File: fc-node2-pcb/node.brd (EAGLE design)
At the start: 50 x 24 mm, 16 parts, among them IC1 HTU21D, J1 AVR_SPI_PRG_62X3_LOCK

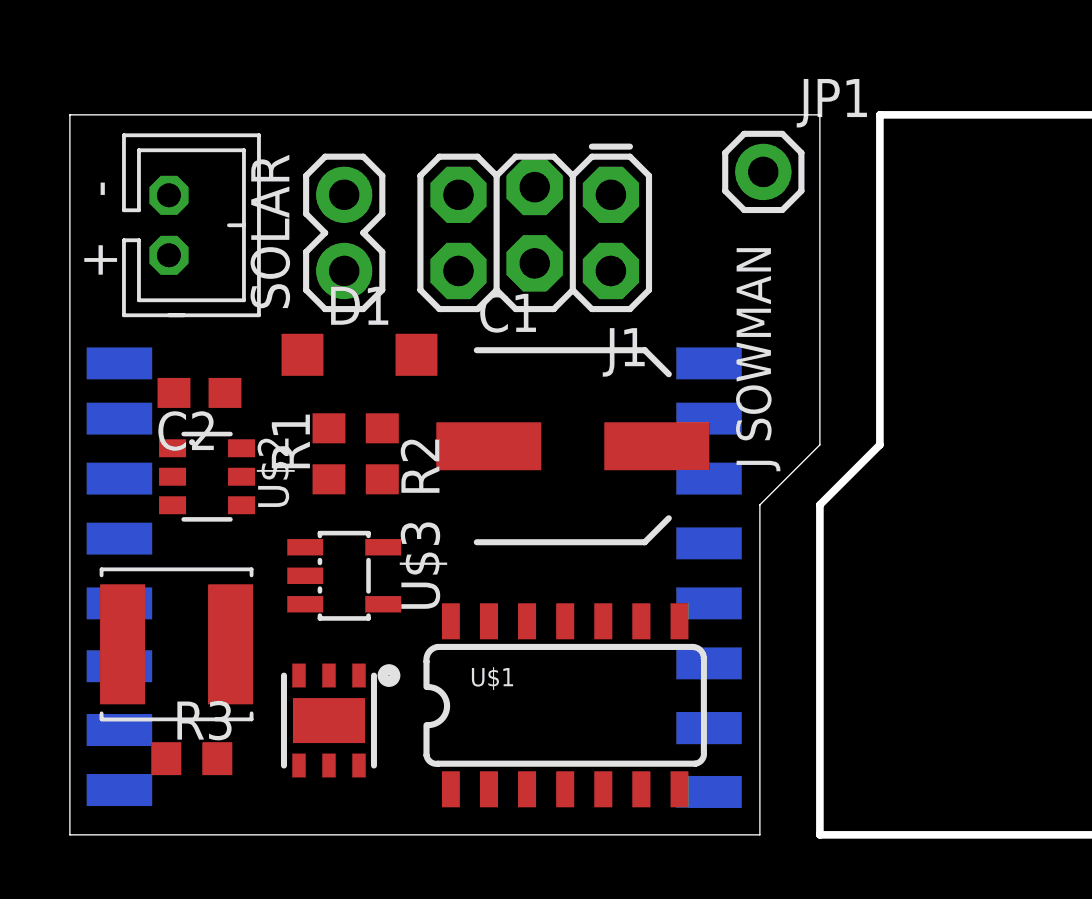
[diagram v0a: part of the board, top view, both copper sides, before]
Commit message: reduced to 23mm, begin routing fc2
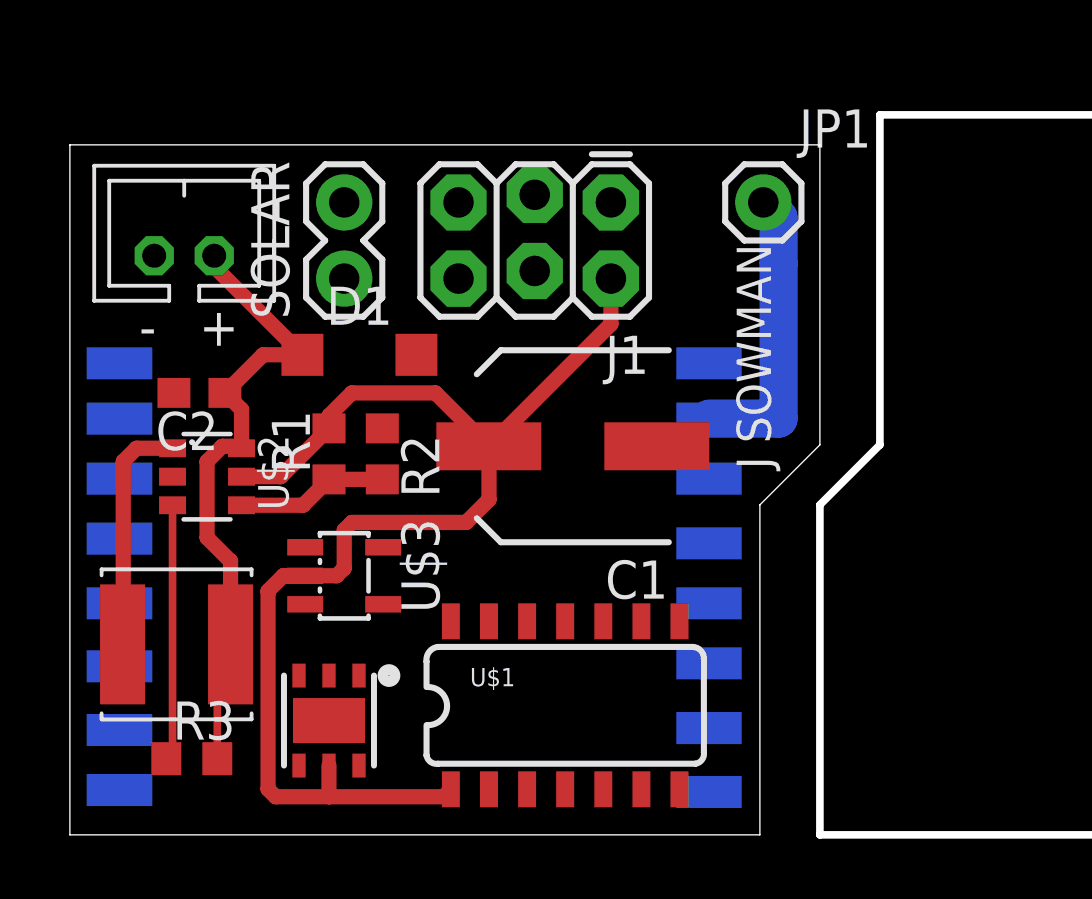
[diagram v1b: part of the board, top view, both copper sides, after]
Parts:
- moved J2 1.14 mm to (3.81, 19.3), turned to 0 degrees
- moved JP1 1.02 mm to (23.1, 21.1)
- moved J1 0.25 mm to (18.0, 21.1)
- moved SOLAR 0.25 mm to (9.14, 18.5)
- turned C1 to 180 degrees
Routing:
- net VCC: track 0.00 -> 43.5 mm
- net VBATT: track 0.00 -> 21.5 mm
- net N$3: track 0.00 -> 9.74 mm
- net EN: track 0.07 -> 8.60 mm
- net N$1: track 0.33 -> 8.26 mm
- net N$2: track 0.00 -> 5.05 mm
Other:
- outline, holes or cut-outs redrawn

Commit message: routed fc2
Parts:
- moved U$3 1.02 mm to (10.2, 8.64), turned to 180 degrees
- moved IC1 0.92 mm to (9.40, 4.32)
- moved U$1 0.51 mm to (16.5, 4.83)
- moved J1 0.51 mm to (18.0, 20.6)
- moved R1 0.25 mm to (8.64, 13.0)
- moved R2 0.25 mm to (10.4, 13.0)
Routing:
- net MOSI: track 0.00 -> 50.5 mm, vias 0 -> 2
- net SCK: track 0.00 -> 50.3 mm, vias 0 -> 2
- net RESET: track 0.00 -> 25.6 mm
- net EN: track 8.60 -> 33.6 mm
- net MISO: track 0.00 -> 21.5 mm, vias 0 -> 1
- net DIO0: track 0.00 -> 20.7 mm, vias 0 -> 1
- net VCC: track 43.5 -> 60.8 mm
- net VBATT: track 21.5 -> 37.9 mm
- net DET: track 0.00 -> 16.0 mm
- net RFM_SS: track 0.00 -> 9.28 mm, vias 0 -> 1
- net N$5: track 0.00 -> 3.54 mm
- net GND: track 0.00 -> 1.36 mm, vias 0 -> 29
- net N$3: track 9.74 -> 8.58 mm
- added copper zone on layer 1, net GND
- added copper zone on layer 16, net GND
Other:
- outline, holes or cut-outs redrawn
- board text added: "APRIL 2015"
- board text added: "J. SOWMAN"
- board text added: "JON SOWMAN"
- board text added: "UKHASnet"
- board text added: "ukhas.net"

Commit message: fc2 decoupling cap
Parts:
- added C3: 100n, rcl:C0603
- moved R3 1.27 mm to (4.06, 3.81)
- moved DF 1.02 mm to (3.56, 7.37)
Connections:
- net GND: now also C3.2
- net VCC: now also C3.1
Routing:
- net GND: track 1.36 -> 5.75 mm, vias 29 -> 32
- net EN: track 33.6 -> 35.6 mm
- net N$1: track 8.26 -> 6.92 mm
- net VBATT: track 37.9 -> 39.2 mm
- net VCC: track 60.8 -> 61.9 mm
- net SCK: track 50.3 -> 49.6 mm
- net MOSI: track 50.5 -> 49.9 mm
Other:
- board text added: "+"
- board text added: "APR 15"
- board text added: "JON"
- board text added: "SOWMAN"
- board text added: "UKHAS"
- board text removed: "J. SOWMAN"
- board text removed: "UKHASnet"

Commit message: fc2 running ok, no rfm yet
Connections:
- new net N$4: U$1.3
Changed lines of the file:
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@@
 <?xml version="1.0" encoding="utf-8"?>
 <!DOCTYPE eagle SYSTEM "eagle.dtd">
-<eagle version="6.6.0">
+<eagle version="6.5.0">
 <drawing>
 <settings>
@@
 <setting verticaltext="up"/>
 </settings>
-<grid distance="0.01" unitdist="inch" unit="inch" style="lines" multiple="1" display="yes" altdistance="0.005" altunitdist="inch" altunit="inch"/>
+<grid distance="0.05" unitdist="inch" unit="inch" style="lines" multiple="1" display="yes" altdistance="0.005" altunitdist="inch" altunit="inch"/>
 <layers>
 <layer number="1" name="Top" color="4" fill="1" visible="yes" active="yes"/>
@@
 <layer number="47" name="Measures" color="7" fill="1" visible="no" active="yes"/>
 <layer number="48" name="Document" color="7" fill="1" visible="no" active="yes"/>
-<layer number="49" name="Reference" color="7" fill="1" visible="yes" active="yes"/>
+<layer number="49" name="Reference" color="7" fill="1" visible="no" active="yes"/>
 <layer number="50" name="dxf" color="7" fill="1" visible="no" active="no"/>
 <layer number="51" name="tDocu" color="6" fill="1" visible="yes" active="yes"/>
@@
 <wire x1="11.557" y1="9.017" x2="12.446" y2="9.906" width="0.254" layer="1"/>
 </signal>
+<signal name="N$4">
+<contactref element="U$1" pad="3"/>
+</signal>
 </signals>

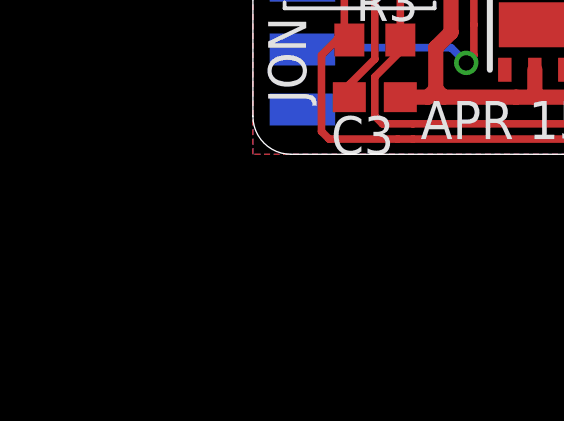
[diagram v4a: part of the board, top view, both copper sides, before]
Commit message: Work on bitbanged firmware for a attiny node
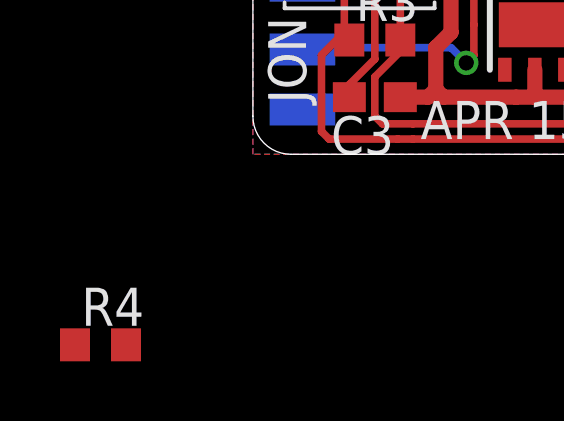
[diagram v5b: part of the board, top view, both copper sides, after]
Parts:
- added R4: (no value), rcl:R0603
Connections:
- new net N$6: U$1.6
- new net N$7: U$4.RESET
- net RFM_SS: now also R4.1
- net VCC: now also R4.2
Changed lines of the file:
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@@
 <element name="IC1" library="Mine" package="DFN6-L" value="HTU21D" x="9.398" y="4.318" rot="R180"/>
 <element name="C3" library="rcl" package="C0603" value="100n" x="4.064" y="1.905" rot="R180"/>
+<element name="R4" library="rcl" package="R0603" value="" x="-5.08" y="-6.35"/>
 </elements>
 <signals>
@@
 <wire x1="4.914" y1="1.905" x2="5.842" y2="1.905" width="0.508" layer="1"/>
 <wire x1="5.842" y1="1.905" x2="6.096" y2="2.159" width="0.508" layer="1"/>
+<contactref element="R4" pad="2"/>
+<wire x1="4.914" y1="1.905" x2="-4.23" y2="-6.35" width="0" layer="19" extent="1-1"/>
 </signal>
 <signal name="N$1">
@@
 <via x="16.51" y="3.556" extent="1-16" drill="0.508"/>
 <wire x1="16.51" y1="3.556" x2="16.51" y2="7.626" width="0.254" layer="1"/>
+<contactref element="R4" pad="1"/>
+<wire x1="-5.93" y1="-6.35" x2="16.51" y2="3.556" width="0" layer="19" extent="1-16"/>
 </signal>
 <signal name="N$3">
@@
 <contactref element="U$1" pad="3"/>
 </signal>
+<signal name="N$6">
+<contactref element="U$1" pad="6"/>
+</signal>
+<signal name="N$7">
+<contactref element="U$4" pad="RESET"/>
+</signal>
 </signals>

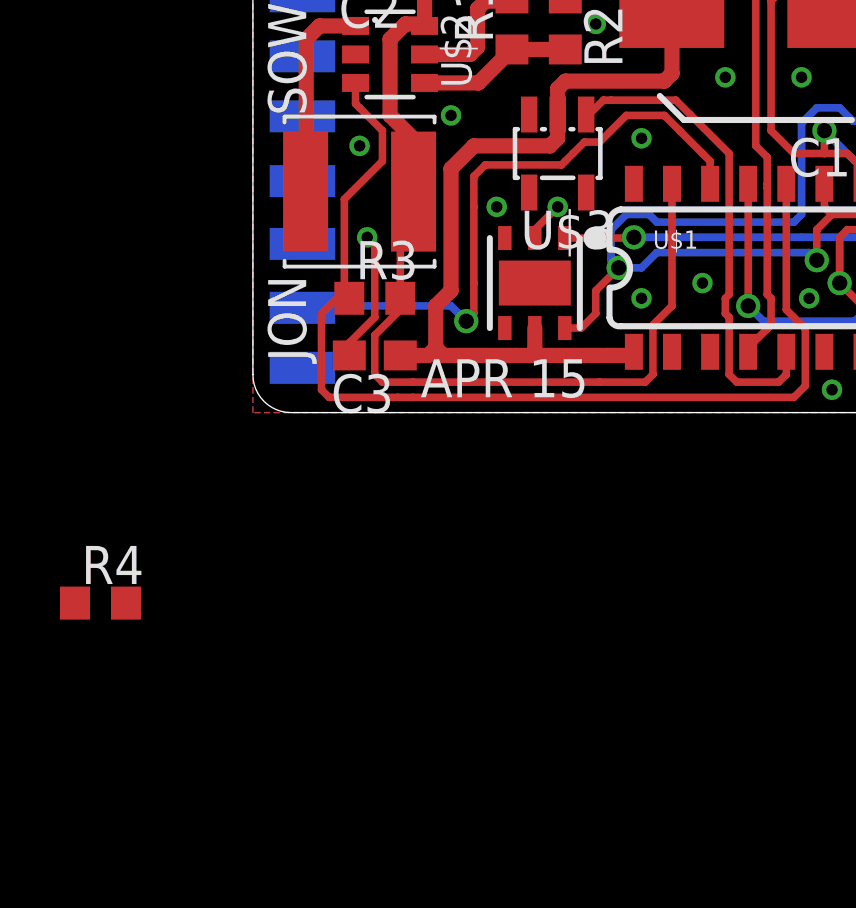
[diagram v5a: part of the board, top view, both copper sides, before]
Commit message: added potential divider for vbatt so we can use internal 1v1 ref
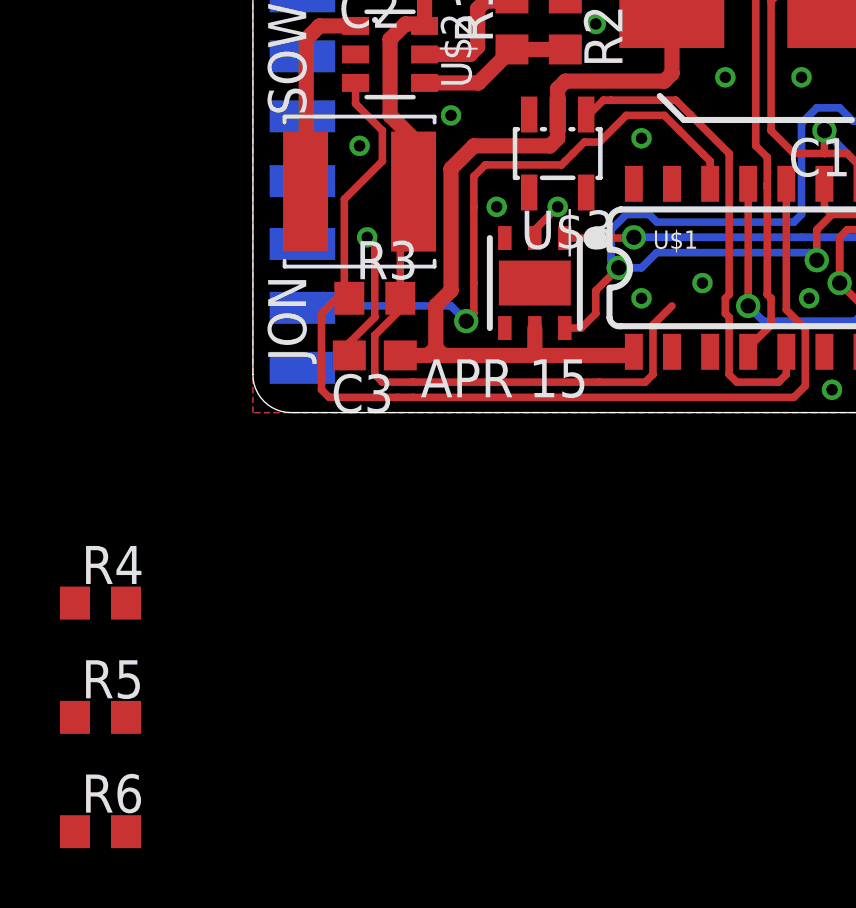
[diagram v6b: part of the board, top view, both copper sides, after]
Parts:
- added R5, R6: (no value), rcl:R0603
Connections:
- new net VSENSE: R5.1, R6.2, U$1.13
- net GND: now also R6.1
- net VBATT: now also R5.2; no longer U$1.13
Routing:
- net VBATT: track 39.2 -> 35.2 mm
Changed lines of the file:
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@@
 <?xml version="1.0" encoding="utf-8"?>
 <!DOCTYPE eagle SYSTEM "eagle.dtd">
-<eagle version="6.5.0">
+<eagle version="7.3.0">
 <drawing>
 <settings>
@@
 <layer number="56" name="wert" color="7" fill="1" visible="no" active="no"/>
 <layer number="57" name="tCAD" color="7" fill="1" visible="no" active="no"/>
-<layer number="90" name="Modules" color="5" fill="1" visible="no" active="yes"/>
+<layer number="90" name="Modules" color="5" fill="1" visible="no" active="no"/>
 <layer number="91" name="Nets" color="2" fill="1" visible="no" active="no"/>
 <layer number="92" name="Busses" color="1" fill="1" visible="no" active="no"/>
@@
 <pass name="Default">
 <param name="RoutingGrid" value="50mil"/>
+<param name="AutoGrid" value="1"/>
+<param name="Efforts" value="0"/>
+<param name="TopRouterVariant" value="1"/>
 <param name="tpViaShape" value="round"/>
 <param name="PrefDir.1" value="|"/>
@@
 <element name="C3" library="rcl" package="C0603" value="100n" x="4.064" y="1.905" rot="R180"/>
 <element name="R4" library="rcl" package="R0603" value="" x="-5.08" y="-6.35"/>
+<element name="R5" library="rcl" package="R0603" value="" x="-5.08" y="-10.16"/>
+<element name="R6" library="rcl" package="R0603" value="" x="-5.08" y="-13.97"/>
 </elements>
 <signals>
@@
 <wire x1="4.064" y1="3.175" x2="4.064" y2="5.588" width="0.254" layer="1"/>
 <wire x1="4.064" y1="5.588" x2="3.81" y2="5.842" width="0.254" layer="1"/>
+<contactref element="R6" pad="1"/>
+<wire x1="3.214" y1="1.905" x2="-5.93" y2="-13.97" width="0" layer="19" extent="1-1"/>
 </signal>
 <signal name="VCC">
@@
 <contactref element="D1" pad="C"/>
 <contactref element="R3" pad="2"/>
-<contactref element="U$1" pad="13"/>
 <wire x1="4.81" y1="19.304" x2="4.81" y2="18.944" width="0.508" layer="1"/>
 <wire x1="4.81" y1="18.944" x2="7.752" y2="16.002" width="0.508" layer="1"/>
@@
 <wire x1="11.557" y1="1.016" x2="5.334" y2="1.016" width="0.254" layer="1"/>
 <wire x1="13.335" y1="1.27" x2="13.335" y2="2.921" width="0.254" layer="1"/>
-<wire x1="13.97" y1="3.556" x2="13.97" y2="7.626" width="0.254" layer="1"/>
 <wire x1="13.97" y1="3.556" x2="13.335" y2="2.921" width="0.254" layer="1"/>
 <wire x1="5.334" y1="1.016" x2="4.318" y2="1.016" width="0.254" layer="1"/>
@@
 <wire x1="4.914" y1="5.908" x2="4.914" y2="6.924" width="0.254" layer="1"/>
 <wire x1="4.914" y1="6.924" x2="5.356" y2="7.366" width="0.254" layer="1"/>
+<contactref element="R5" pad="2"/>
+<wire x1="4.318" y1="1.016" x2="-4.23" y2="-10.16" width="0" layer="19" extent="1-1"/>
 </signal>
 <signal name="RFM_SS">
@@
 <contactref element="U$4" pad="RESET"/>
 </signal>
+<signal name="VSENSE">
+<contactref element="U$1" pad="13"/>
+<contactref element="R5" pad="1"/>
+<contactref element="R6" pad="2"/>
+<wire x1="-5.93" y1="-10.16" x2="13.97" y2="7.626" width="0" layer="19" extent="1-1"/>
+<wire x1="-4.23" y1="-13.97" x2="-5.93" y2="-10.16" width="0" layer="19" extent="1-1"/>
+</signal>
 </signals>
